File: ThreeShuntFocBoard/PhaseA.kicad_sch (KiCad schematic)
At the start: 40 parts, among them J10 Conn_01x01, Q1 MMBT5551L, Q10 IRF540N, Q2 SS8050, Q3 SS8550, Q4 SS8550, Q5 SS8550, Q6 SS8550, Q7 IRF540N, Q8 IRF540N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

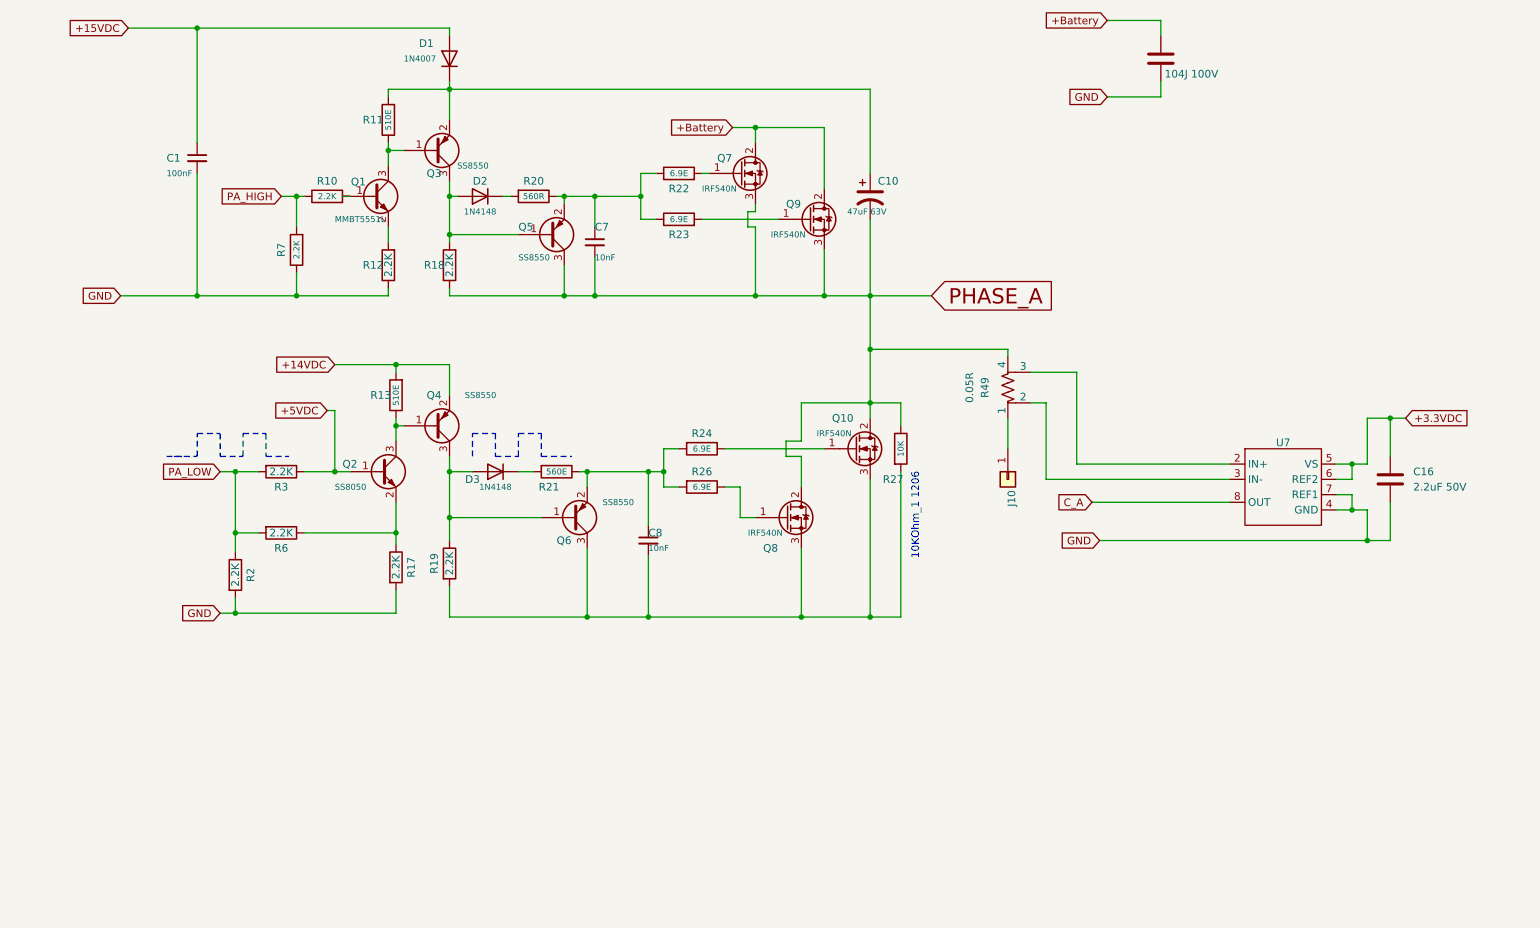
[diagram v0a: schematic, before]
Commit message: commit 2:  Updated Power Supply, Safety Fuse, Phase Design, and Hall Sensor Circuit
for more details read ChangesDetial.txt in same folder.
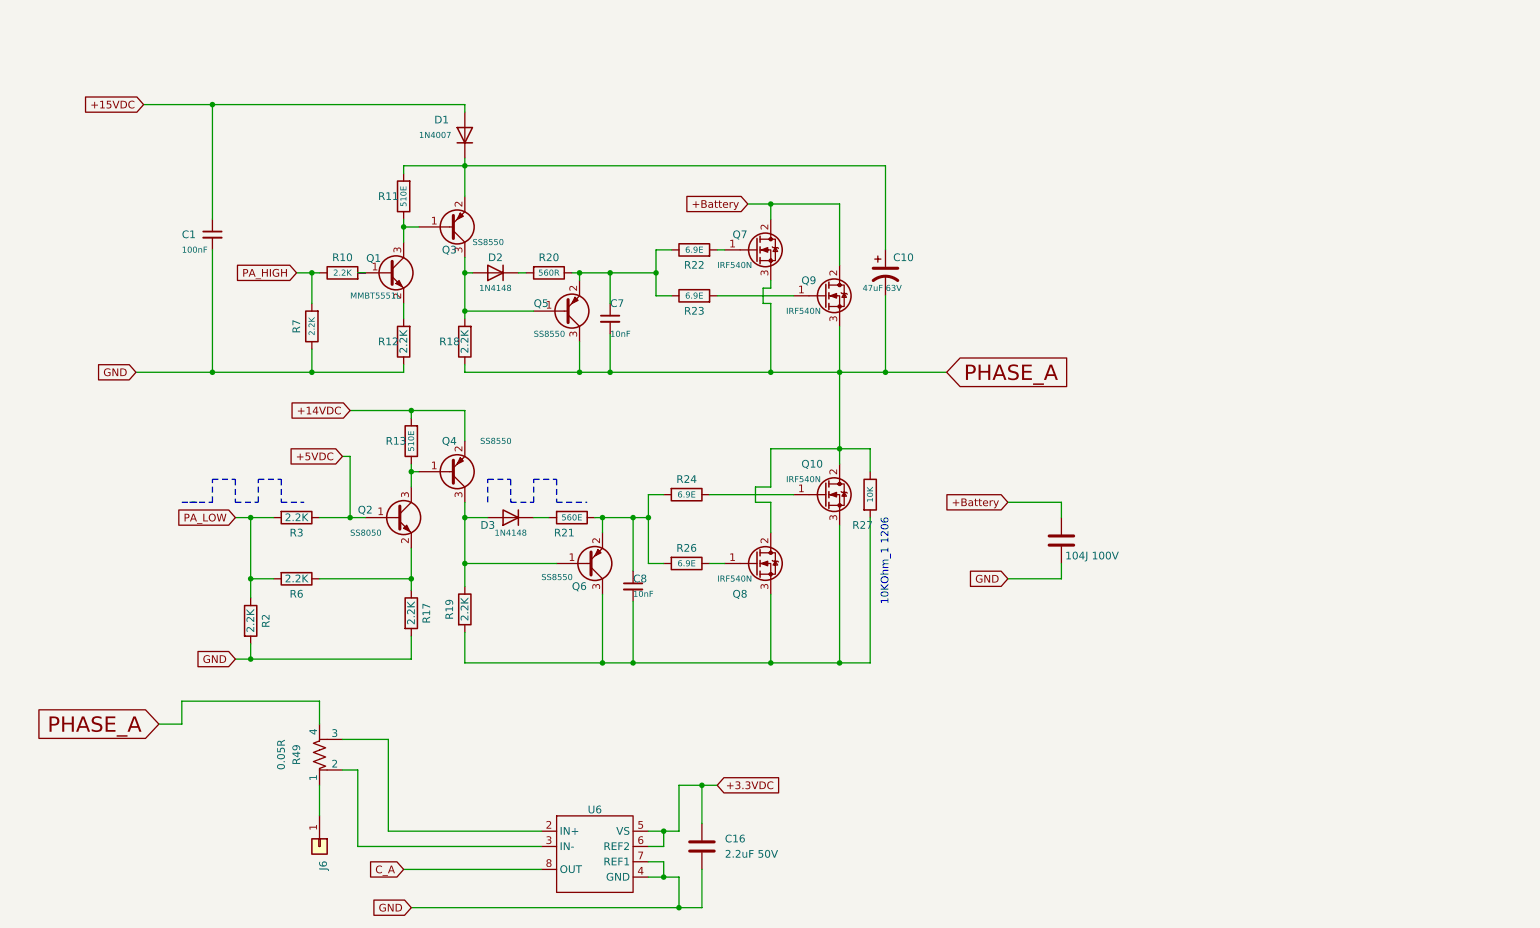
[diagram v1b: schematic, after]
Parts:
- removed J10: Conn_01x01, Footprints:Powe_pad, symbol Connector_Generic:Conn_01x01
- removed U7: ~, symbol Symbol_lib:INA240
- added J6: Conn_01x01, Footprints:Powe_pad, symbol Connector_Generic:Conn_01x01
- added U6: ~, symbol Symbol_lib:INA240
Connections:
- net +3.3VDC: now also U6.5 (VS), U6.6 (REF2)
- net C_A: now also U6.8 (OUT)
- net GND: now also U6.4 (GND), U6.7 (REF1)
- net at R49.1: now also J6.1 (Pin_1)
- net at R49.2: now also U6.3 (IN-)
- net at R49.3: now also U6.2 (IN+)

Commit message: Commit 3: Assigned STM32G431C6Tx (LQFP-48) pins as per the shared Excel, peripheral connections WIP, Phase C current sensing removed due to ADC group limitations
read attach excel files and changesDetails.txt file for more detail
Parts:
- added C27: 100nF, Footprints:104J_100V, symbol Device:C
- added R1: 56K, symbol Device:R
- added R25: 10K, Footprints:1206_R, symbol Device:R
- added R5: 2.2k, symbol Device:R
- added TH1: 10K, symbol Device:Thermistor_NTC
- U6: value ~ -> INA240
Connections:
- net +3.3VDC: now also TH1.1
- net GND: now also C27.2, R25.2, R5.2
- net PHASE_A: now also R1.1
- new net PhaseA_Temp: R25.1, TH1.2
- new net PhaseA_Voltage: C27.1, R1.2, R5.1
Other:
- note added: "MotorPhaseA"
- moved on the sheet: J6

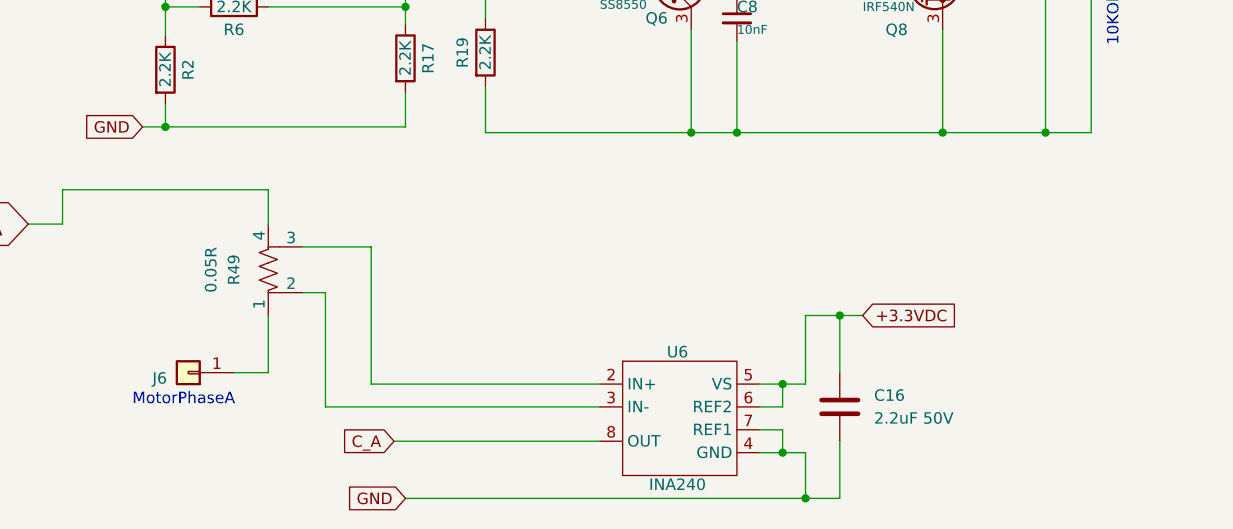
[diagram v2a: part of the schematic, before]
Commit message: Commit 5: Improved power integrity and ADC accuracy.
for more details read changesDetail.txt file
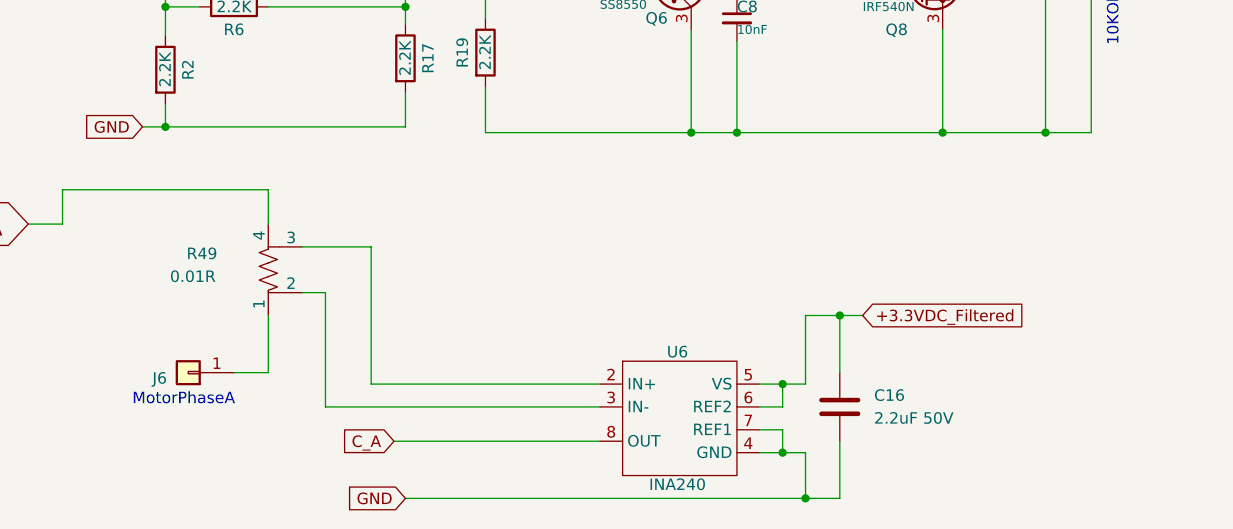
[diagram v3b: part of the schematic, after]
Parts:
- R49: value 0.05R -> 0.01R
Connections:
- net +3.3VDC: no longer C16.1, U6.5 (VS), U6.6 (REF2)
- new net +3.3VDC_Filtered: C16.1, U6.5 (VS), U6.6 (REF2)
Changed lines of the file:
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@@
-		)
-	)
-	(global_label "+3.3VDC"
-		(shape input)
-		(at 134.62 147.32 0)
-		(fields_autoplaced yes)
-		(effects
-			(font
-				(size 1.27 1.27)
-			)
-			(justify left)
-		)
-		(property "Intersheetrefs" "${INTERSHEET_REFS}"
-			(at 145.83 147.32 0)
-			(effects
-				(font
-					(size 1.27 1.27)
-				)
-				(justify left)
-				(hide yes)
-			)
 		)
 	)
@@
 		)
 	)
+	(global_label "+3.3VDC_Filtered"
+		(shape input)
+		(at 134.62 147.32 0)
+		(fields_autoplaced yes)
+		(effects
+			(font
+				(size 1.27 1.27)
+			)
+			(justify left)
+		)
+		(property "Intersheetrefs" "${INTERSHEET_REFS}"
+			(at 153.9943 147.32 0)
+			(effects
+				(font
+					(size 1.27 1.27)
+				)
+				(justify left)
+				(hide yes)
+			)
+		)
+	)
 	(global_label "PhaseA_Temp"
 		(shape input)
@@
 		(dnp no)
 		(property "Reference" "R49"
-			(at 64.77 142.24 90)
-			(effects
-				(font
-					(size 1.27 1.27)
-				)
-			)
-		)
-		(property "Value" "0.05R"
-			(at 62.23 142.24 90)
-			(effects
-				(font
+			(at 61.214 140.462 0)
+			(effects
+				(font
+					(size 1.27 1.27)
+				)
+			)
+		)
+		(property "Value" "0.01R"
+			(at 60.198 143.002 0)
+			(effects
+				(font
